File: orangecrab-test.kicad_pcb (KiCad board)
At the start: 2 copper layers, 50.8 x 77.5 mm, 66 parts, among them J1 Conn_01x16, J2 Conn_01x12, J3 USB_B_Micro, J4 JTAG, SW1 SW_Push, U1 DAC53608RTET, U2 MCP23S08T-E-ML, U3 93C46B/SN, U4 FT232HL-REEL, Y1 12MHz

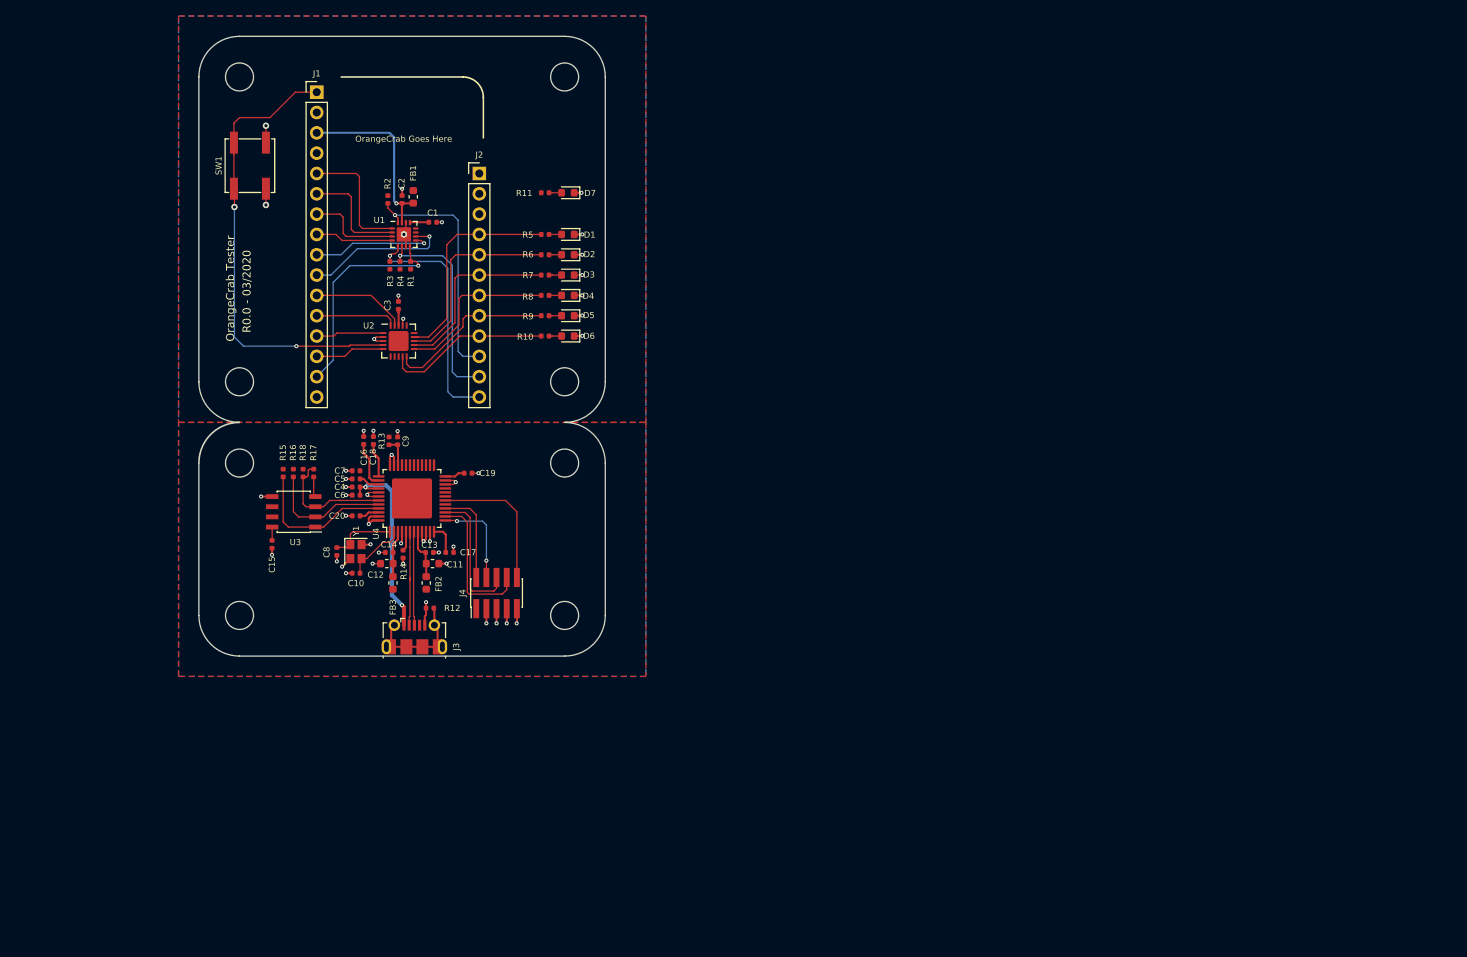
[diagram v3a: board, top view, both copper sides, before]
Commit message: added 2 layers for board/pogo alignment. battery circuit
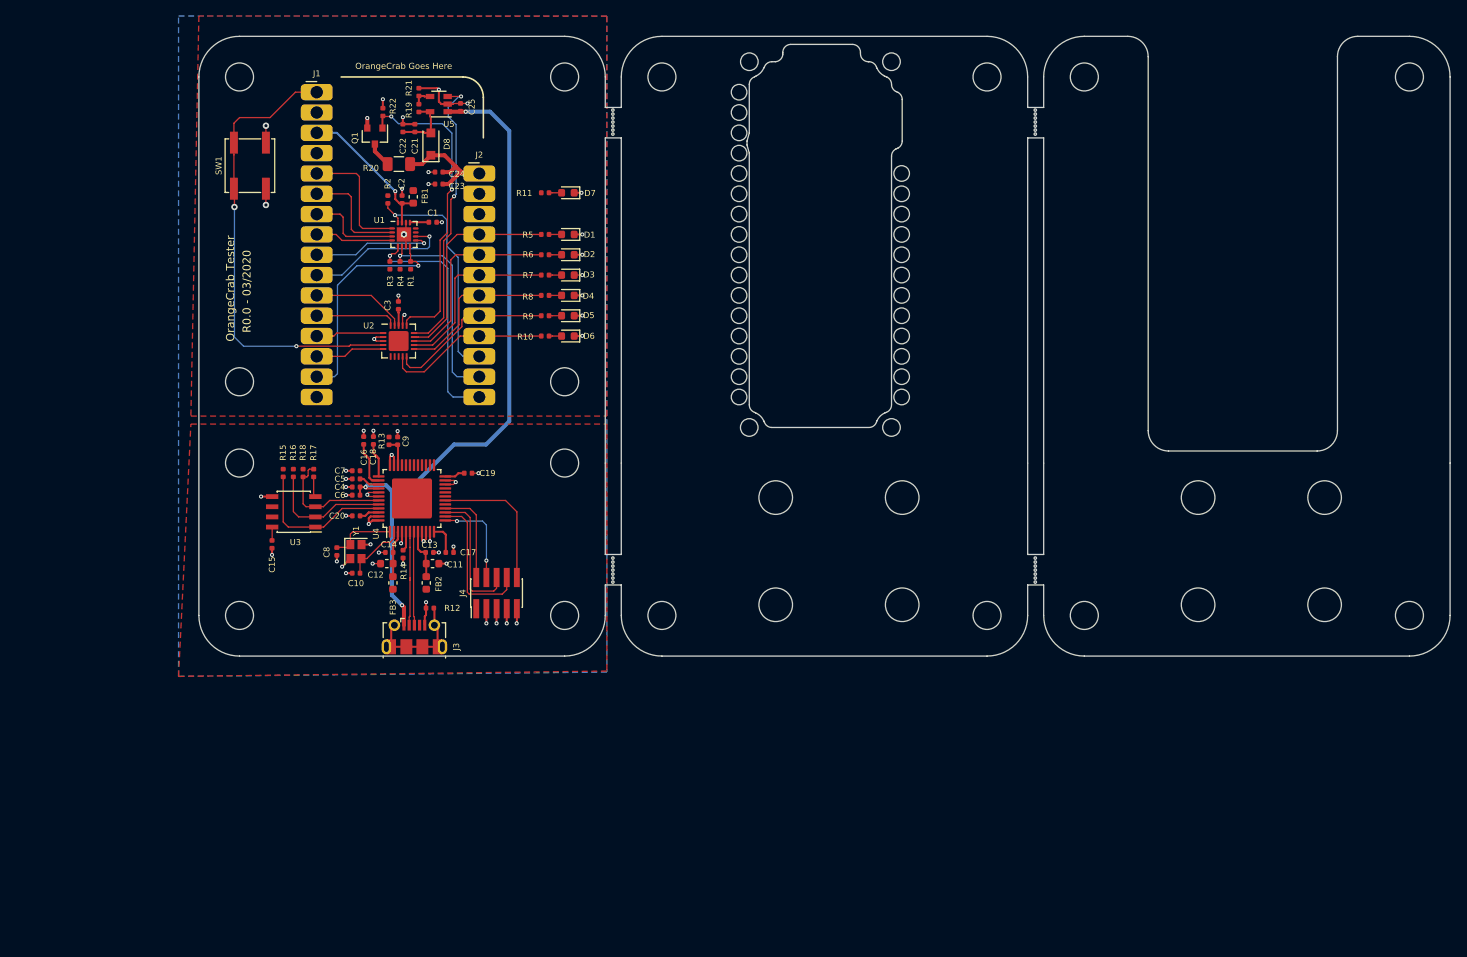
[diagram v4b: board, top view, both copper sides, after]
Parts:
- added C21: 4.7uF, Capacitor_SMD:C_0402_1005Metric, F.Cu at (123.5, 39.4)
- added C22: .1uF, Capacitor_SMD:C_0402_1005Metric, F.Cu at (122.0, 39.4)
- added C23: 4.7uF, Capacitor_SMD:C_0402_1005Metric, F.Cu at (126.5, 46.4)
- added C24: .1uF, Capacitor_SMD:C_0402_1005Metric, F.Cu at (126.5, 44.9)
- added C25: .1uF, Capacitor_SMD:C_0402_1005Metric, F.Cu at (129.2, 36.8)
- added D8: PMEG3015EH,115, Diode_SMD:D_SOD-123F, F.Cu at (125.5, 41.4)
- added H1: MountingHole, MountingHole:MountingHole_3.5mm, F.Cu at (201.1, 93.7)
- added H1: MountingHole, MountingHole:MountingHole_3.5mm, F.Cu at (201.1, 39.7)
- added H1: MountingHole, MountingHole:MountingHole_3.5mm, F.Cu at (201.1, 38.2)
- added H1: MountingHole, MountingHole:MountingHole_3.5mm, F.Cu at (201.1, 39.2)
- added H1: MountingHole, MountingHole:MountingHole_3.5mm, F.Cu at (201.1, 38.7)
- added H1: MountingHole, MountingHole:MountingHole_3.5mm, F.Cu at (201.1, 94.7)
- added H1: MountingHole, MountingHole:MountingHole_3.5mm, F.Cu at (148.3, 96.2)
- added H1: MountingHole, MountingHole:MountingHole_3.5mm, F.Cu at (148.3, 93.7)
- added H1: MountingHole, MountingHole:MountingHole_3.5mm, F.Cu at (148.3, 93.2)
- added H1: MountingHole, MountingHole:MountingHole_3.5mm, F.Cu at (148.3, 95.7)
- added H1: MountingHole, MountingHole:MountingHole_3.5mm, F.Cu at (148.3, 94.2)
- added H1: MountingHole, MountingHole:MountingHole_3.5mm, F.Cu at (201.1, 93.2)
- added H1: MountingHole, MountingHole:MountingHole_3.5mm, F.Cu at (148.3, 95.2)
- added H1: MountingHole, MountingHole:MountingHole_3.5mm, F.Cu at (148.3, 94.7)
- added H1: MountingHole, MountingHole:MountingHole_3.5mm, F.Cu at (148.3, 40.2)
- added H1: MountingHole, MountingHole:MountingHole_3.5mm, F.Cu at (148.3, 39.7)
- added H1: MountingHole, MountingHole:MountingHole_3.5mm, F.Cu at (148.3, 39.2)
- added H1: MountingHole, MountingHole:MountingHole_3.5mm, F.Cu at (148.3, 38.7)
- added H1: MountingHole, MountingHole:MountingHole_3.5mm, F.Cu at (148.3, 38.2)
- added H1: MountingHole, MountingHole:MountingHole_3.5mm, F.Cu at (148.3, 37.7)
- added H1: MountingHole, MountingHole:MountingHole_3.5mm, F.Cu at (148.3, 37.2)
- added H1: MountingHole, MountingHole:MountingHole_3.5mm, F.Cu at (207.2, 33.0)
- added H1: MountingHole, MountingHole:MountingHole_3.5mm, F.Cu at (201.1, 40.2)
- added H1: MountingHole, MountingHole:MountingHole_3.5mm, F.Cu at (154.4, 33.0)
- added H1: MountingHole, MountingHole:MountingHole_3.5mm, F.Cu at (201.1, 37.7)
- added H1: MountingHole, MountingHole:MountingHole_3.5mm, F.Cu at (201.1, 95.7)
- added H1: MountingHole, MountingHole:MountingHole_3.5mm, F.Cu at (201.1, 96.2)
- added H1: MountingHole, MountingHole:MountingHole_3.5mm, F.Cu at (201.1, 37.2)
- added H1: MountingHole, MountingHole:MountingHole_3.5mm, F.Cu at (201.1, 94.2)
- added H1: MountingHole, MountingHole:MountingHole_3.5mm, F.Cu at (201.1, 95.2)
- added H2: MountingHole, MountingHole:MountingHole_3.5mm, F.Cu at (247.8, 33.0)
- added H2: MountingHole, MountingHole:MountingHole_3.5mm, F.Cu at (195.0, 33.0)
- added H3: MountingHole, MountingHole:MountingHole_3.5mm, F.Cu at (168.6, 85.6)
- added H3: MountingHole, MountingHole:MountingHole_3.5mm, F.Cu at (154.4, 100.3)
- added H3: MountingHole, MountingHole:MountingHole_3.5mm, F.Cu at (168.6, 99.0)
- added H3: MountingHole, MountingHole:MountingHole_3.5mm, F.Cu at (184.4, 99.0)
- added H3: MountingHole, MountingHole:MountingHole_3.5mm, F.Cu at (184.4, 85.6)
- added H3: MountingHole, MountingHole:MountingHole_3.5mm, F.Cu at (221.4, 85.6)
- added H3: MountingHole, MountingHole:MountingHole_3.5mm, F.Cu at (237.2, 85.6)
- added H3: MountingHole, MountingHole:MountingHole_3.5mm, F.Cu at (237.2, 99.0)
- added H3: MountingHole, MountingHole:MountingHole_3.5mm, F.Cu at (221.4, 99.0)
- added H3: MountingHole, MountingHole:MountingHole_3.5mm, F.Cu at (207.2, 100.3)
- added H4: MountingHole, MountingHole:MountingHole_3.5mm, F.Cu at (247.8, 100.3)
- added H4: MountingHole, MountingHole:MountingHole_3.5mm, F.Cu at (195.0, 100.3)
- added Q1: DMG2302UK-7, Package_TO_SOT_SMD:SOT-23, F.Cu at (118.5, 40.4)
- added R19: 402k, Resistor_SMD:R_0402_1005Metric, F.Cu at (124.0, 36.9)
- added R20: 82R, Resistor_SMD:R_1206_3216Metric, F.Cu at (121.5, 43.9)
- added R21: 169k, Resistor_SMD:R_0402_1005Metric, F.Cu at (124.0, 34.9)
- added R22: 4.7K, Resistor_SMD:R_0402_1005Metric, F.Cu at (119.5, 37.4)
- added REF**: MountingHole_2.2mm_M2_DIN965, MountingHole:MountingHole_2.2mm_M2_DIN965, F.Cu at (184.4, 73.0)
- added REF**: MountingHole_2.2mm_M2_DIN965, MountingHole:MountingHole_2.2mm_M2_DIN965, F.Cu at (184.4, 50.2)
- added REF**: MountingHole_2.2mm_M2_DIN965, MountingHole:MountingHole_2.2mm_M2_DIN965, F.Cu at (184.4, 47.6)
- added REF**: MountingHole_2.2mm_M2_DIN965, MountingHole:MountingHole_2.2mm_M2_DIN965, F.Cu at (184.4, 45.1)
- added REF**: MountingHole_2.2mm_M2_DIN965, MountingHole:MountingHole_2.2mm_M2_DIN965, F.Cu at (164.0, 73.0)
- added REF**: MountingHole_2.2mm_M2_DIN965, MountingHole:MountingHole_2.2mm_M2_DIN965, F.Cu at (164.0, 70.5)
- added REF**: MountingHole_2.2mm_M2_DIN965, MountingHole:MountingHole_2.2mm_M2_DIN965, F.Cu at (164.0, 67.9)
- added REF**: MountingHole_2.2mm_M2_DIN965, MountingHole:MountingHole_2.2mm_M2_DIN965, F.Cu at (164.0, 65.4)
- added REF**: MountingHole_2.2mm_M2_DIN965, MountingHole:MountingHole_2.2mm_M2_DIN965, F.Cu at (164.0, 62.9)
- added REF**: MountingHole_2.2mm_M2_DIN965, MountingHole:MountingHole_2.2mm_M2_DIN965, F.Cu at (164.0, 60.3)
- added REF**: MountingHole_2.2mm_M2_DIN965, MountingHole:MountingHole_2.2mm_M2_DIN965, F.Cu at (164.0, 57.8)
- added REF**: MountingHole_2.2mm_M2_DIN965, MountingHole:MountingHole_2.2mm_M2_DIN965, F.Cu at (184.4, 70.5)
- added REF**: MountingHole_2.2mm_M2_DIN965, MountingHole:MountingHole_2.2mm_M2_DIN965, F.Cu at (164.0, 55.2)
- added REF**: MountingHole_2.2mm_M2_DIN965, MountingHole:MountingHole_2.2mm_M2_DIN965, F.Cu at (164.0, 52.7)
- added REF**: MountingHole_2.2mm_M2_DIN965, MountingHole:MountingHole_2.2mm_M2_DIN965, F.Cu at (164.0, 50.2)
- added REF**: MountingHole_2.2mm_M2_DIN965, MountingHole:MountingHole_2.2mm_M2_DIN965, F.Cu at (164.0, 47.6)
- added REF**: MountingHole_2.2mm_M2_DIN965, MountingHole:MountingHole_2.2mm_M2_DIN965, F.Cu at (164.0, 45.1)
- added REF**: MountingHole_2.2mm_M2_DIN965, MountingHole:MountingHole_2.2mm_M2_DIN965, F.Cu at (164.0, 42.5)
- added REF**: MountingHole_2.2mm_M2_DIN965, MountingHole:MountingHole_2.2mm_M2_DIN965, F.Cu at (164.0, 40.0)
- added REF**: MountingHole_2.2mm_M2_DIN965, MountingHole:MountingHole_2.2mm_M2_DIN965, F.Cu at (164.0, 37.5)
- added REF**: MountingHole_2.2mm_M2_DIN965, MountingHole:MountingHole_2.2mm_M2_DIN965, F.Cu at (164.0, 34.9)
- added REF**: MountingHole_2.2mm_M2_DIN965, MountingHole:MountingHole_2.2mm_M2_DIN965, F.Cu at (165.3, 76.8)
- added REF**: MountingHole_2.2mm_M2_DIN965, MountingHole:MountingHole_2.2mm_M2_DIN965, F.Cu at (184.4, 67.9)
- added REF**: MountingHole_2.2mm_M2_DIN965, MountingHole:MountingHole_2.2mm_M2_DIN965, F.Cu at (183.1, 76.8)
- added REF**: MountingHole_2.2mm_M2_DIN965, MountingHole:MountingHole_2.2mm_M2_DIN965, F.Cu at (183.1, 31.1)
- added REF**: MountingHole_2.2mm_M2_DIN965, MountingHole:MountingHole_2.2mm_M2_DIN965, F.Cu at (165.3, 31.1)
- added REF**: MountingHole_2.2mm_M2_DIN965, MountingHole:MountingHole_2.2mm_M2_DIN965, F.Cu at (184.4, 65.4)
- added REF**: MountingHole_2.2mm_M2_DIN965, MountingHole:MountingHole_2.2mm_M2_DIN965, F.Cu at (184.4, 62.9)
- added REF**: MountingHole_2.2mm_M2_DIN965, MountingHole:MountingHole_2.2mm_M2_DIN965, F.Cu at (184.4, 60.3)
- added REF**: MountingHole_2.2mm_M2_DIN965, MountingHole:MountingHole_2.2mm_M2_DIN965, F.Cu at (184.4, 57.8)
- added REF**: MountingHole_2.2mm_M2_DIN965, MountingHole:MountingHole_2.2mm_M2_DIN965, F.Cu at (184.4, 55.2)
- added REF**: MountingHole_2.2mm_M2_DIN965, MountingHole:MountingHole_2.2mm_M2_DIN965, F.Cu at (184.4, 52.7)
- added U5: TPS76301DBVR, Package_TO_SOT_SMD:SOT-23-5, F.Cu at (126.5, 36.4)
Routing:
- net +5V: track 24.5 -> 87.8 mm, vias 2 -> 3
- net Net-(Q1-Pad1): track 0.00 -> 39.2 mm, vias 0 -> 2
- net Net-(U2-Pad15): track 0.00 -> 35.7 mm, vias 0 -> 2
- net /VBAT: track 0.00 -> 14.9 mm
- net GND: track 66.3 -> 81.0 mm, vias 48 -> 55
- net /4V: track 0.00 -> 7.65 mm
- net /AREF: track 22.8 -> 18.7 mm
- net Net-(Q1-Pad3): track 0.00 -> 3.56 mm
- net Net-(R19-Pad2): track 0.00 -> 2.46 mm
- net /~CLR_IO5: track 30.4 -> 29.6 mm
- net /~LDAC_IO0: track 27.4 -> 28.2 mm
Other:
- board size 50.8 x 77.5 mm -> 156.4 x 77.5 mm

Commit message: Add regulator input pulldown and add silkscreen bling
Signed-off-by: Michael Welling <mwelling@ieee.org>
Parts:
- removed H7, H8: MountingHole, MountingHole:MountingHole_3.5mm
- added G***: LOGO, orangecrab-test:logo, F.Cu at (225.4, 92.1)
- added R23: 4.7K, Resistor_SMD:R_0402_1005Metric, F.Cu at (109.0, 66.9)
- added REF**: ESD-Logo_8.9x8mm_SilkScreen, Symbol:ESD-Logo_8.9x8mm_SilkScreen, F.Cu at (188.0, 77.5)
- added REF**: OSHW-Symbol_8.9x8mm_SilkScreen, Symbol:OSHW-Symbol_8.9x8mm_SilkScreen, F.Cu at (187.9, 106.9)
- moved H3 38.8 mm to (148.3, 132.0)
- moved REF** 38.8 mm to (164.0, 101.0)
- moved REF** 38.8 mm to (164.0, 90.8)
- moved C11 38.8 mm to (105.4, 126.9)
- moved C12 38.8 mm to (99.7, 126.9)
- moved C2 38.8 mm to (101.6, 81.4)
- moved D3 38.8 mm to (122.3, 90.8)
- moved H1 38.8 mm to (128.0, 129.2)
- moved H1 38.8 mm to (128.0, 126.7)
- moved H1 38.8 mm to (128.0, 126.2)
- moved H1 38.8 mm to (128.0, 128.7)
- moved H1 38.8 mm to (128.0, 127.2)
- moved H1 38.8 mm to (128.0, 128.2)
- moved H1 38.8 mm to (128.0, 127.7)
- moved H1 38.8 mm to (128.0, 73.2)
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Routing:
- net Net-(R23-Pad2): track 35.7 -> 36.8 mm
- net GND: track 81.0 -> 81.9 mm, vias 55 -> 56
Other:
- board text added: "Battery connector goes on this side."
- board text added: "OrangeCrab Test Fixture"

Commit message: r0.0 release:  - Design review  - Fixed minor error  - Validate BOM  - Generate and package gerbers for fabrication
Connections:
- C15 pad 1: Net-(C15-Pad1) -> +3.3VA
- U3 pad 8: Net-(C15-Pad1) -> +3.3VA
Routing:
- net +3.3VA: track 11.5 -> 13.2 mm
- net Net-(C15-Pad1): track 1.68 -> 0.00 mm
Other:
- rule solder_mask_min_width: 0.25 -> 0.02
